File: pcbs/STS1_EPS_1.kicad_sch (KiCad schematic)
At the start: 7 parts, among them J1 Conn_02x06_Counter_Clockwise, J2 Conn_02x06_Counter_Clockwise, Q1 SI7272DP-T1-GE3, Q2 SI7135DP-T1-GE3, U1 LTC4020EUHFPBF, U2 BQ29209DRBT, U3 MAX11632EEGT

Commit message: Worked on STS1_EPS.
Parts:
- removed J1, J2: Conn_02x06_Counter_Clockwise, STS_Connector:M808661205, symbol Connector_Generic:Conn_02x06_Counter_Clockwise
- removed Q1: SI7272DP-T1-GE3, SI7288DPT1GE3, symbol STS_Transistor_FET:SI7272DP-T1-GE3
- removed Q2: SI7135DP-T1-GE3, STS_Package_SO:POWERPAK_SO8_single, symbol STS_Transistor_FET:SI7135DP-T1-GE3
- removed U1: LTC4020EUHFPBF, STS_Package_DFN_QFN:AD_QFN-38_UHF, symbol STS_Battery_Management:LTC4020EUHFPBF
- removed U2: BQ29209DRBT, STS_Package_VSON:TI_VSON8, symbol STS_Battery_Management:BQ29209DRBT
- removed U3: MAX11632EEGT, STS_Package_QSOP:MAX_QSOP24, symbol STS_Analog_ADC:MAX11632EEGT
- added J2: Inter-EPS, symbol Connector_Generic:Conn_02x06_Odd_Even
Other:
- added sheet Battery (STS1_EPS_BATTERY.kicad_sch)
- added sheet Battery Charge Controller (STS1_EPS_BCC.kicad_sch)
- added sheet Cubesat Bus Interface (STS1_EPS_CSBI.kicad_sch)
- added sheet Solar Cell Connectors (STS1_EPS_SC_Connectors.kicad_sch)

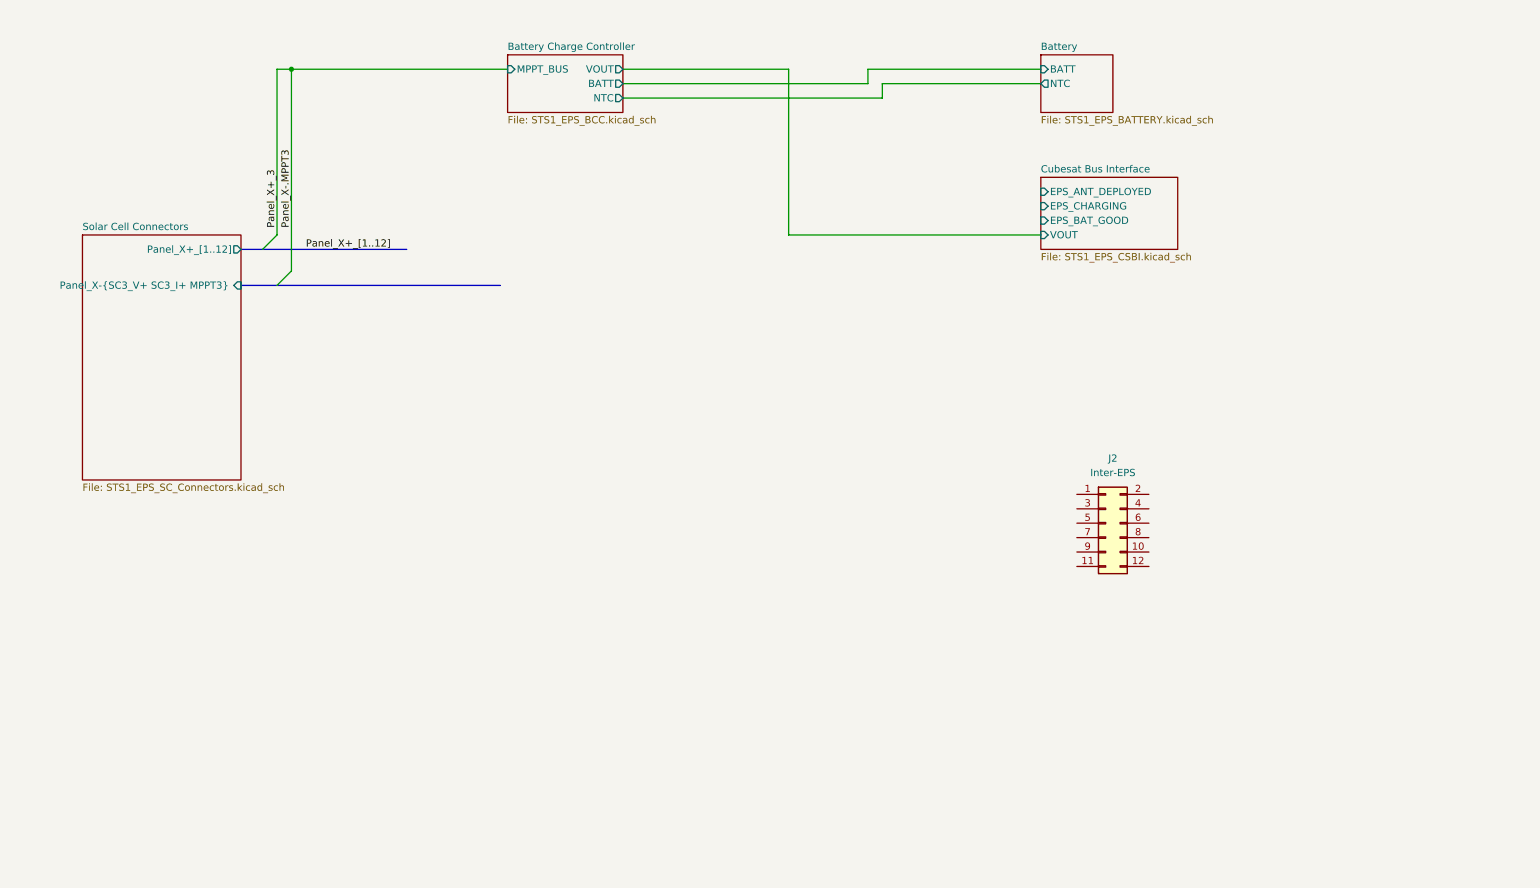
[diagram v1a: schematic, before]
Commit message: Worked on STS1_EPS_1.
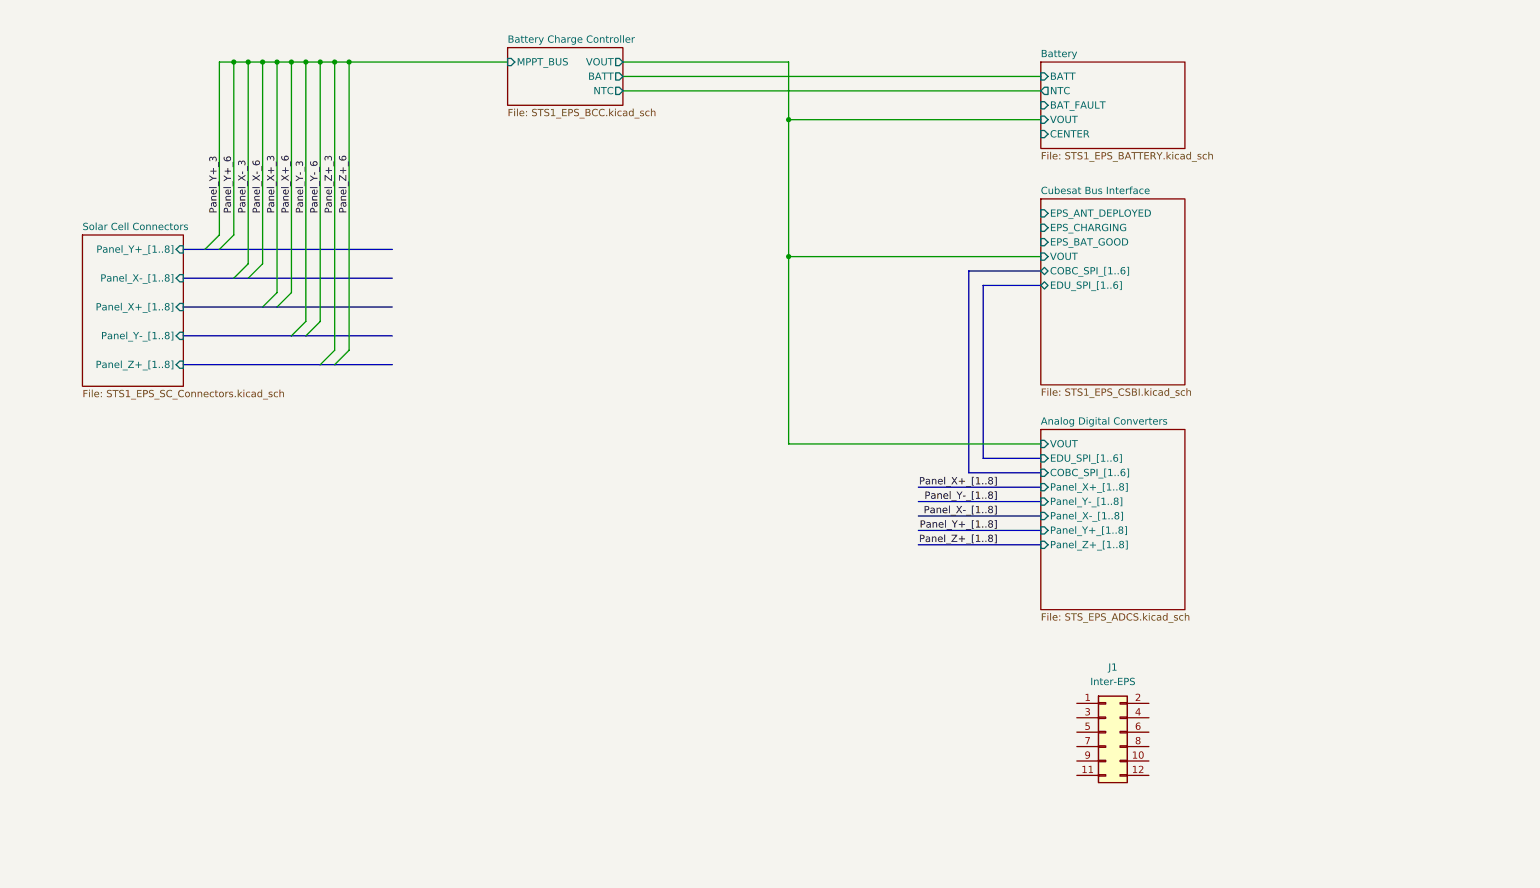
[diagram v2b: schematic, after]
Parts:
- renumbered J2 to J1
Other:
- added sheet Analog Digital Converters (STS_EPS_ADCS.kicad_sch)
- sheet Battery ports: added BAT_FAULT, CENTER, VOUT; removed none
- sheet Cubesat Bus Interface ports: added COBC_SPI_[1..6], EDU_SPI_[1..6]; removed none
- sheet Solar Cell Connectors ports: added Panel_X+_[1..8], Panel_X-_[1..8], Panel_Y+_[1..8], Panel_Y-_[1..8], Panel_Z+_[1..8]; removed Panel_X+_[1..12], Panel_X-{SC3_V+ SC3_I+ MPPT3} 
- moved on the sheet: J1

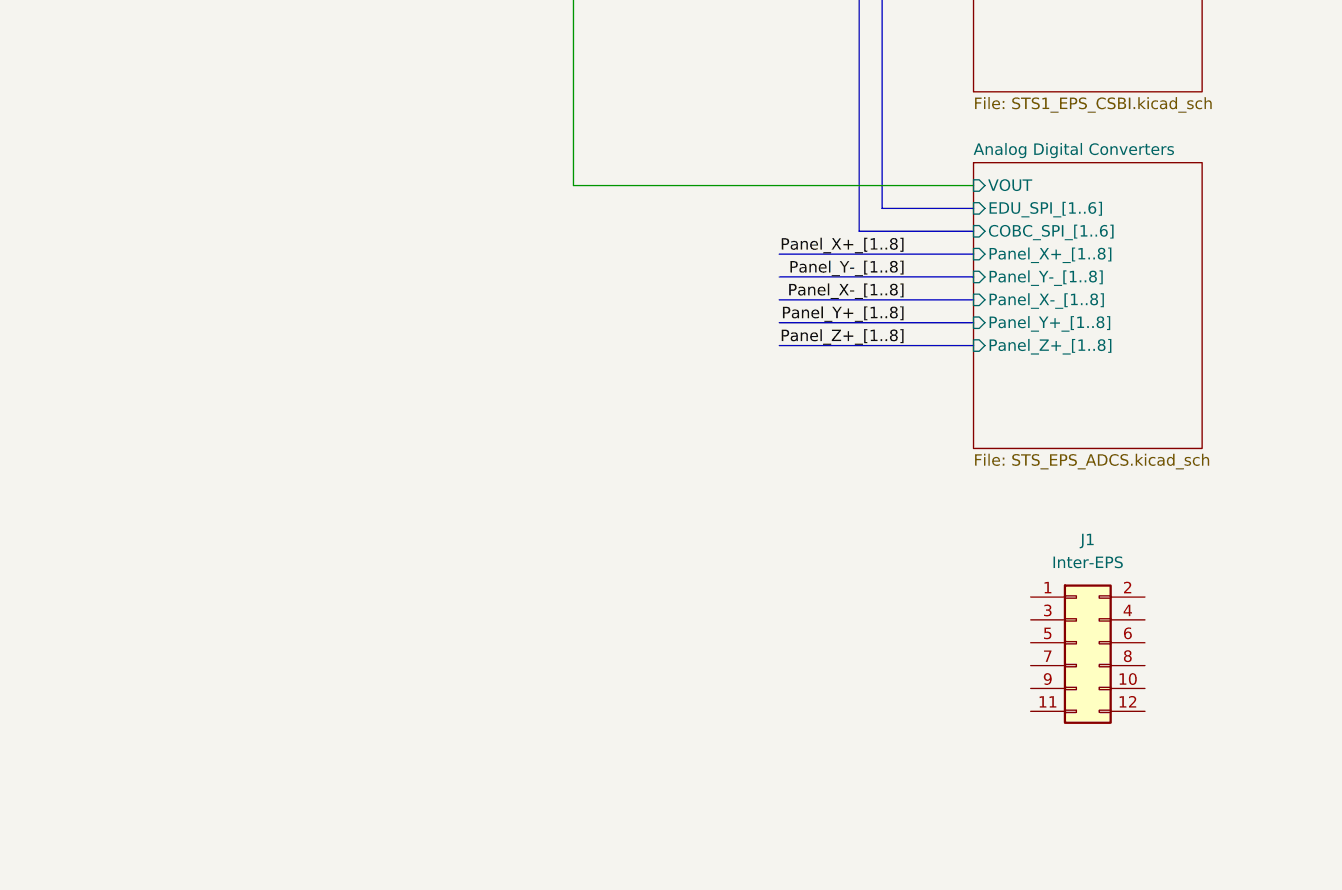
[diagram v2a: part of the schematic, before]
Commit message: Worked on STS_EPS_1.
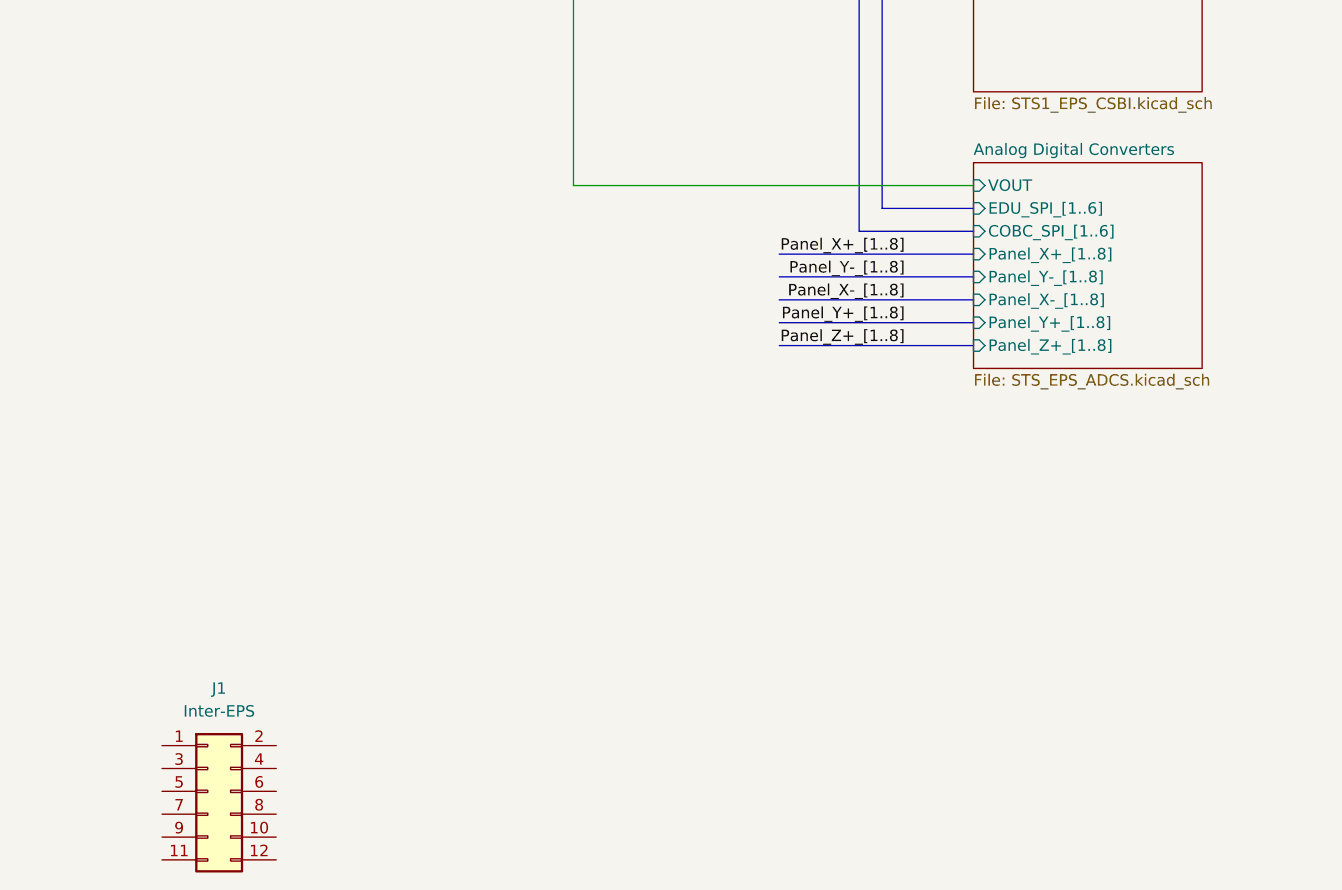
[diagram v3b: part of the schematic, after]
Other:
- moved on the sheet: J1
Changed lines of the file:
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@@
     (effects (font (size 1.27 1.27)) (justify left bottom))
   )
-  (symbol (lib_id "Connector_Generic:Conn_02x06_Odd_Even") (at 199.39 139.7 0) (unit 1)
+  (symbol (lib_id "Connector_Generic:Conn_02x06_Odd_Even") (at 102.87 156.21 0) (unit 1)
     (in_bom yes) (on_board yes) (fields_autoplaced)
-    (property "Reference" "J1" (id 0) (at 200.66 128.27 0))
-    (property "Value" "Inter-EPS" (id 1) (at 200.66 130.81 0))
-    (property "Footprint" "" (id 2) (at 199.39 139.7 0)
+    (property "Reference" "J1" (id 0) (at 104.14 144.78 0))
+    (property "Value" "Inter-EPS" (id 1) (at 104.14 147.32 0))
+    (property "Footprint" "" (id 2) (at 102.87 156.21 0)
       (effects (font (size 1.27 1.27)) hide)
     )
-    (property "Datasheet" "~" (id 3) (at 199.39 139.7 0)
+    (property "Datasheet" "~" (id 3) (at 102.87 156.21 0)
       (effects (font (size 1.27 1.27)) hide)
     )
@@
     )
   )
-  (sheet (at 187.96 86.36) (size 25.4 31.75) (fields_autoplaced)
+  (sheet (at 187.96 86.36) (size 25.4 22.86) (fields_autoplaced)
     (stroke (width 0.1524) (type solid) (color 0 0 0 0))
     (fill (color 0 0 0 0.0000))
@@
       (effects (font (size 1.27 1.27)) (justify left bottom))
     )
-    (property "Sheet file" "STS_EPS_ADCS.kicad_sch" (id 1) (at 187.96 118.6946 0)
+    (property "Sheet file" "STS_EPS_ADCS.kicad_sch" (id 1) (at 187.96 109.8046 0)
       (effects (font (size 1.27 1.27)) (justify left top))
     )

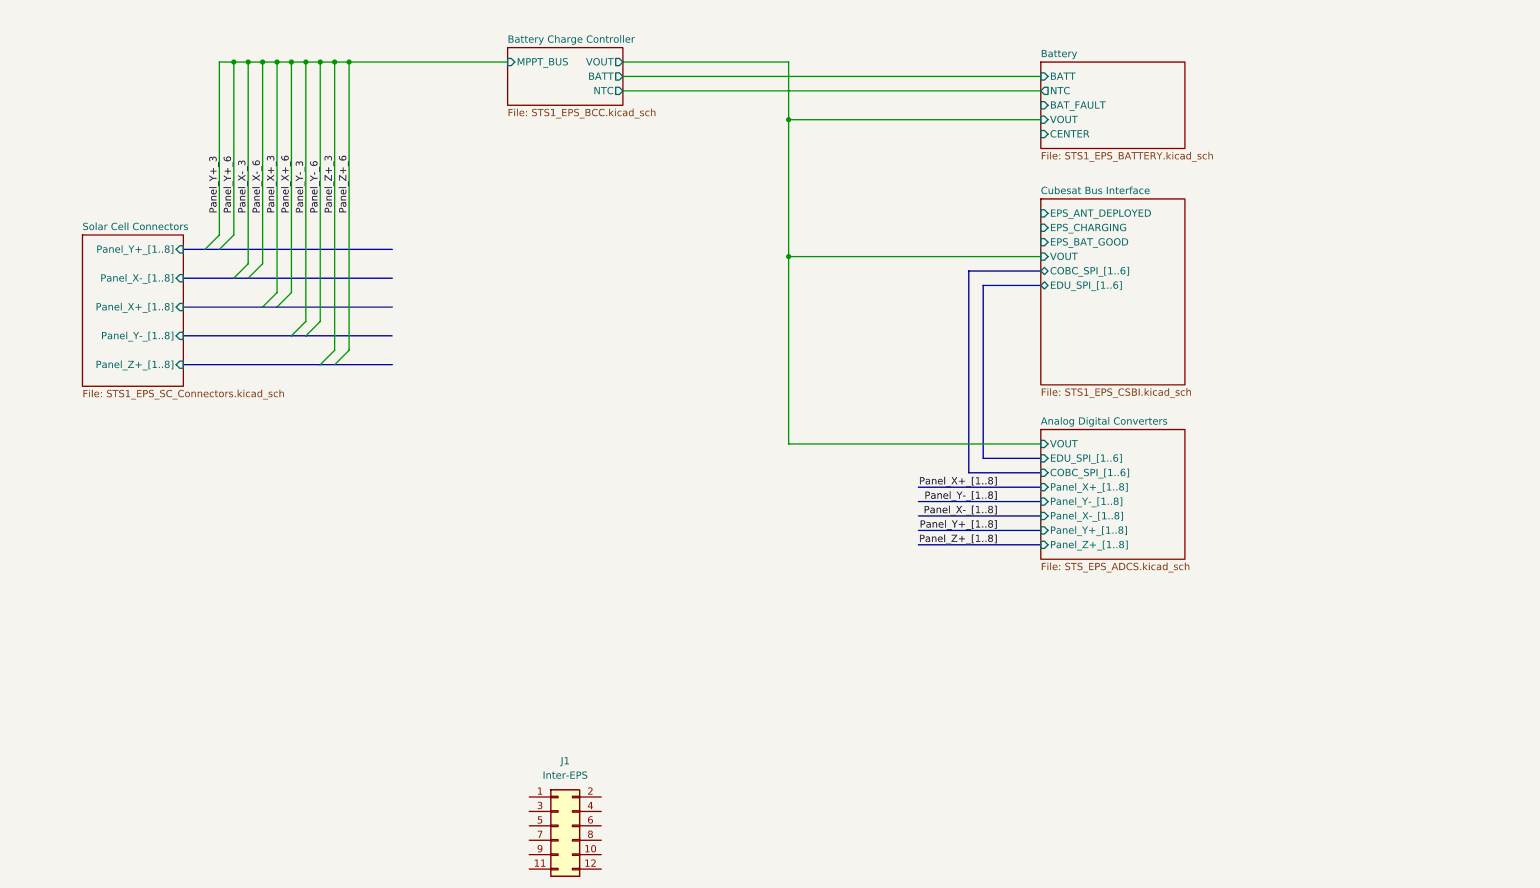
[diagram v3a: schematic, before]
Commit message: Worked on STS1_EPS_1.
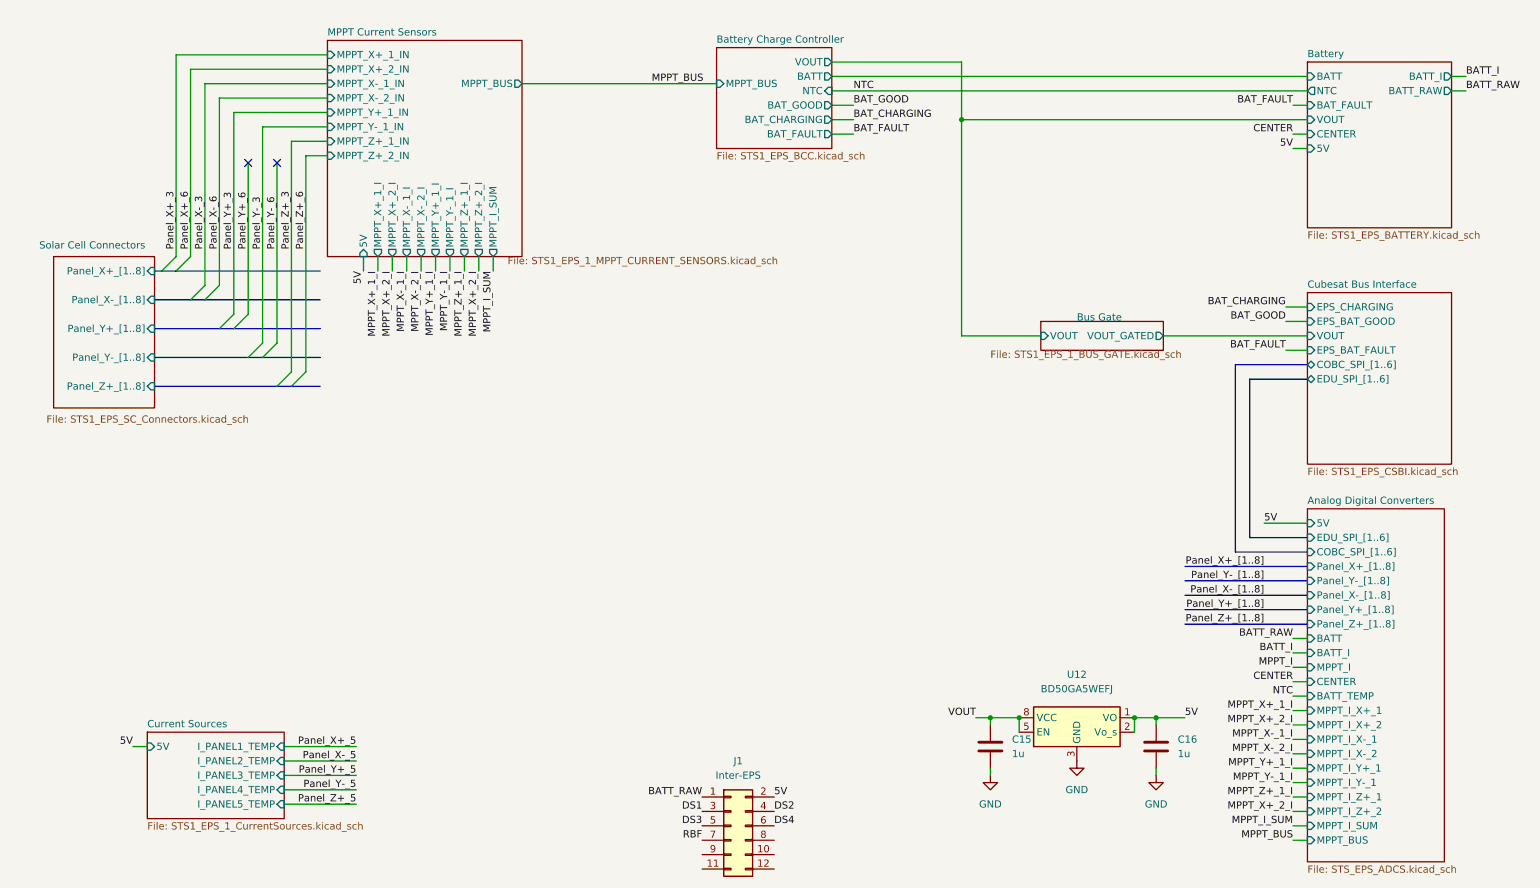
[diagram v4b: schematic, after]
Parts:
- added C15, C16: 1u, Capacitor_SMD:C_0805_2012Metric, symbol Device:C
- added U12: BD50GA5WEFJ, Package_SO:HTSOP-8-1EP_3.9x4.9mm_P1.27mm_EP2.4x3.2mm, symbol Regulator_Linear:BD50GA5WEFJ
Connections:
- net BATT_RAW: now reaches J1.1 (Pin_1)
- net 5V: now reaches J1.2 (Pin_2)
- net 5V: now also C16.1, U12.1 (VO), U12.2 (Vo_s)
- net DS1: now reaches J1.3 (Pin_3)
- net DS2: now reaches J1.4 (Pin_4)
- net DS3: now reaches J1.5 (Pin_5)
- net DS4: now reaches J1.6 (Pin_6)
- net RBF: now reaches J1.7 (Pin_7)
- new net GND: C15.2, C16.2, U12.3 (GND), U12.4 (GND), U12.6 (GND), U12.7 (GND), U12.9 (GND)
- new net VOUT: C15.1, U12.5 (EN), U12.8 (VCC)
- no-connect marks 0 -> 2
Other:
- added sheet Bus Gate (STS1_EPS_1_BUS_GATE.kicad_sch)
- added sheet Current Sources (STS1_EPS_1_CurrentSources.kicad_sch)
- added sheet MPPT Current Sensors (STS1_EPS_1_MPPT_CURRENT_SENSORS.kicad_sch)
- sheet Analog Digital Converters ports: added 5V, BATT, BATT_I, BATT_TEMP, CENTER, MPPT_BUS, MPPT_I, MPPT_I_SUM, MPPT_I_X+_1, MPPT_I_X+_2, MPPT_I_X-_1, MPPT_I_X-_2, MPPT_I_Y+_1, MPPT_I_Y-_1, MPPT_I_Z+_1, MPPT_I_Z+_2; removed VOUT
- sheet Battery ports: added 5V, BATT_I, BATT_RAW; removed none
- sheet Battery Charge Controller ports: added BAT_CHARGING, BAT_FAULT, BAT_GOOD; removed none
- sheet Cubesat Bus Interface ports: added EPS_BAT_FAULT; removed EPS_ANT_DEPLOYED
- moved on the sheet: J1
